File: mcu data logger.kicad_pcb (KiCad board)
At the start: 2 copper layers, 50.6 x 31.6 mm, 29 parts, among them J1 Conn_01x04_Pin, J2 Conn_01x09_Pin, J3 Conn_01x04_Pin, J4 Conn_02x03_Odd_Even, U1 24LC1025, U2 DS1337S_, U3 24LC1025, U4 ATMEGA328P-AU, Y1 32.768 KHz, Y2 16 MHz

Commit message: completed wiring
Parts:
- turned R4 to 180 degrees
- turned Y2 to 180 degrees
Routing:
- net /VCC: track 0.00 -> 118.1 mm, vias 0 -> 2
- net /SCK: track 0.00 -> 111.7 mm, vias 0 -> 8
- net GND: track 0.00 -> 71.6 mm
- net /SDA: track 0.00 -> 65.4 mm, vias 0 -> 6
- net Net-(BT1-+): track 0.00 -> 57.9 mm, vias 0 -> 2
- net /D2: track 0.00 -> 32.2 mm, vias 0 -> 1
- net Net-(U4-PB7): track 0.00 -> 32.0 mm, vias 0 -> 2
- net /MOSI: track 0.00 -> 31.6 mm
- net /D3: track 0.00 -> 29.9 mm, vias 0 -> 2
- net Net-(U4-PB6): track 0.00 -> 28.1 mm
- net /TX: track 0.00 -> 27.6 mm, vias 0 -> 2
- net /RX: track 0.00 -> 26.3 mm, vias 0 -> 2
- net /RESET: track 0.00 -> 24.9 mm, vias 0 -> 2
- net /D4: track 0.00 -> 24.7 mm, vias 0 -> 2
- net /MISO: track 0.00 -> 22.8 mm, vias 0 -> 1
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
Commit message: completed routing
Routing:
- net GND: track 71.6 -> 118.5 mm, vias 0 -> 14
- net /VCC: track 118.1 -> 142.7 mm
- net /SCK: track 111.7 -> 119.9 mm, vias 8 -> 9
- net Net-(BT1-+): track 57.9 -> 65.8 mm, vias 2 -> 4
- net /SDA: track 65.4 -> 68.1 mm, vias 6 -> 7
- net /D4: track 24.7 -> 26.8 mm
- net /RESET: track 24.9 -> 26.7 mm
- net /MISO: track 22.8 -> 24.2 mm
- net Net-(U2-SQW/~INT): track 10.8 -> 9.82 mm
- net /RX: track 26.3 -> 25.4 mm
- net /TX: track 27.6 -> 28.1 mm
- added copper zone on F.Cu, net /VCC
- added copper zone on B.Cu, net GND

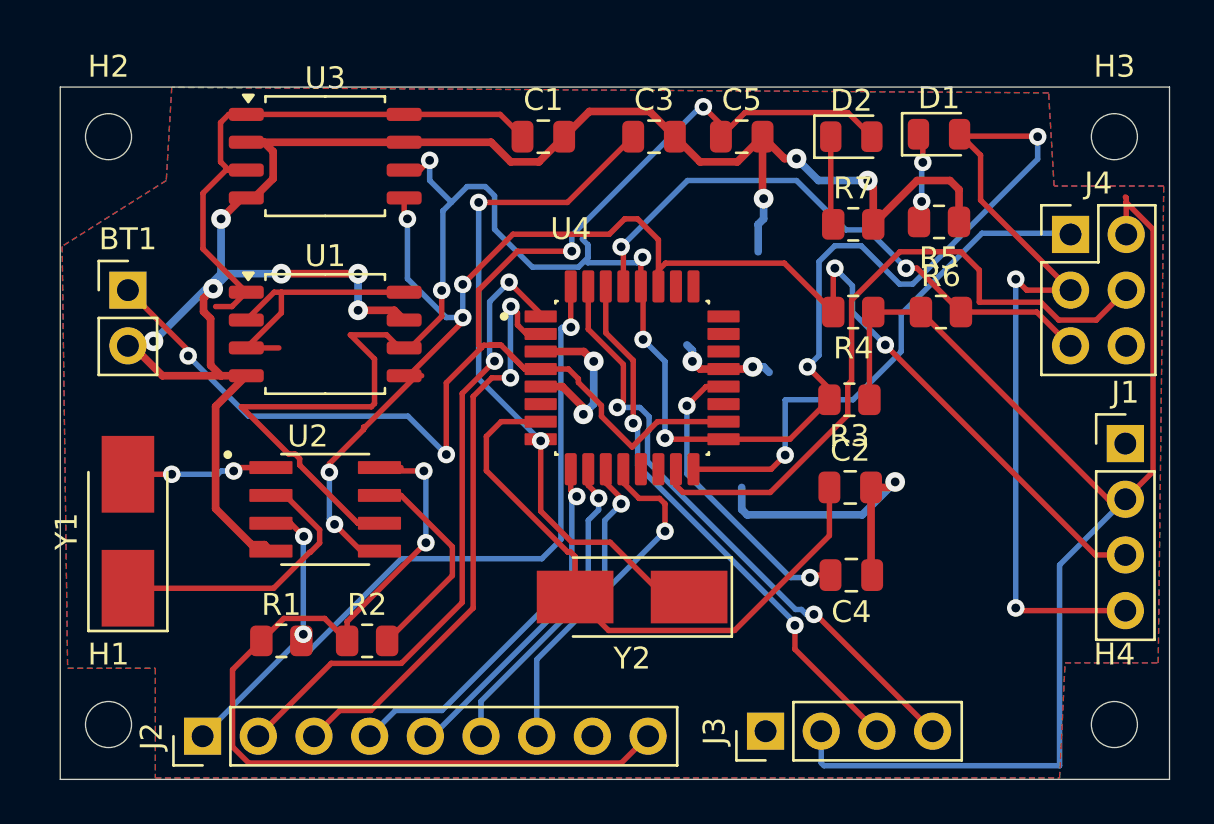
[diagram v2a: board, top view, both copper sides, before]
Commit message: completed silkscreen printing for board
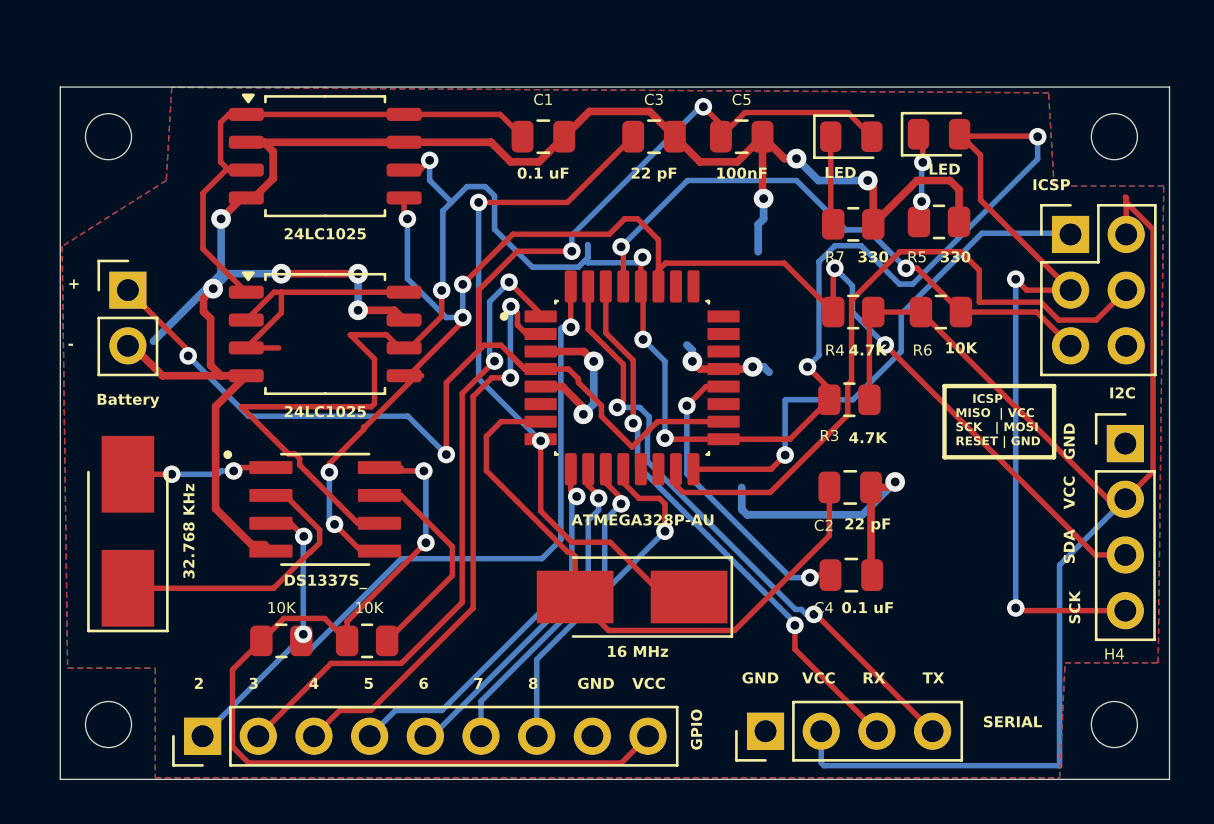
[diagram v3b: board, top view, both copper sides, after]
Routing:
- net /VCC: track 142.7 -> 141.1 mm
- net GND: track 118.5 -> 116.8 mm, vias 14 -> 13
- net Net-(BT1-+): track 65.8 -> 65.2 mm
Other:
- board text added: "+"
- board text added: "-"
- board text added: "2"
- board text added: "3"
- board text added: "4"
- board text added: "5"
- board text added: "6"
- board text added: "7"
- board text added: "8"
- board text added: "GND"
- board text added: "GPIO"
- board text added: "I2C"
- board text added: "ICSP"
- board text added: "ICSP MISO | VCC SCK | MOSI RESET | GND"
- board text added: "RX"
- board text added: "SCK"
- board text added: "SDA"
- board text added: "SERIAL"
- board text added: "TX"
- board text added: "VCC"
